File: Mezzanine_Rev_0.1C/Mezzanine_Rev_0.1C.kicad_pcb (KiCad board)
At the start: 2 copper layers, 170 x 85.1 mm, 62 parts, among them J1 QBUS_DWK_64Pin_MBT, J2 DIP20 Header, J3 DIP20 Header, J4 IDC-64M, J5 IDC-16M, J6 IDC-20M, J7 Conn_01x03_Pin, J8 PLD-16R, U1 1533LI1, U10 74LS07, U11 74LS74, U2 1533TM2, U3 1533LA8, U4 CD74HCT4067M, U5 1533LE4, U6 1533AP6, U7 1533AP6, U8 74LS07, U9 74LS07

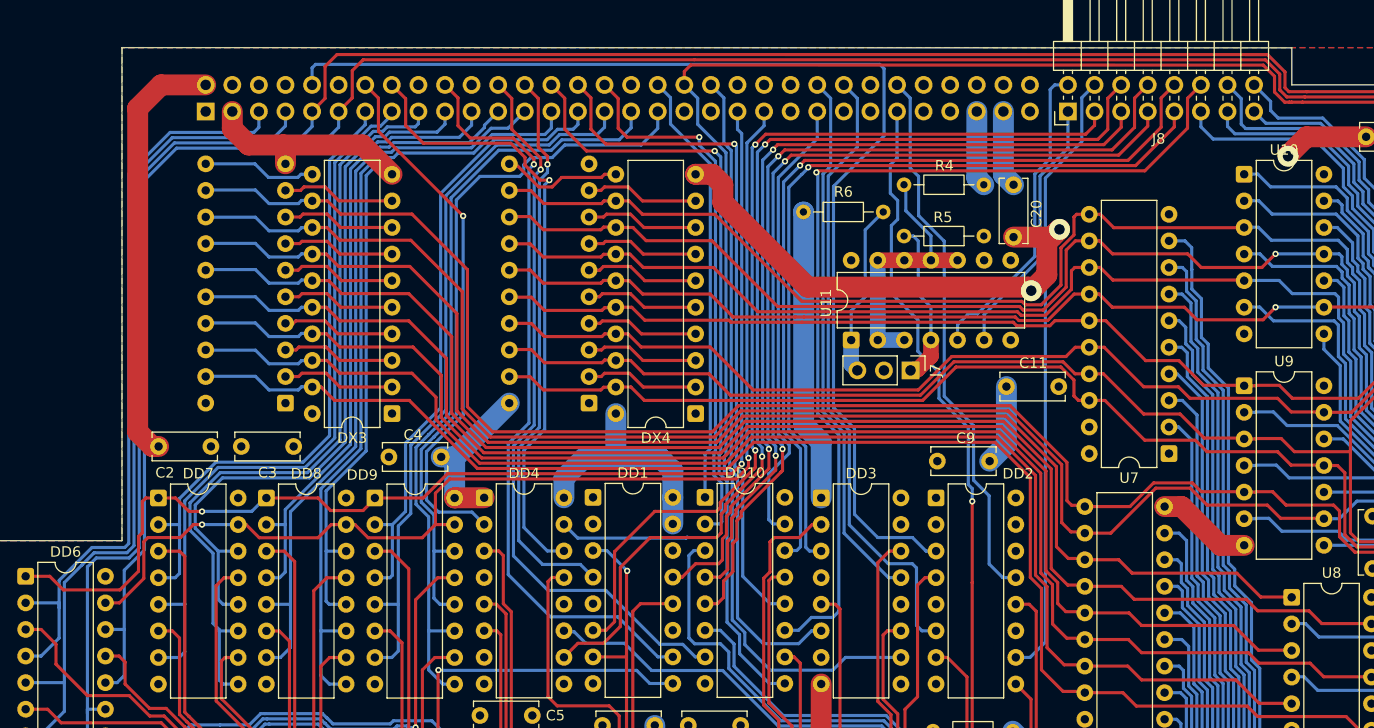
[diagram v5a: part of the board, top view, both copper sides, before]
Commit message: Mezzanine: More layout improvements
Repositioned DX4, allowing for further power tracks connectivity improvements.
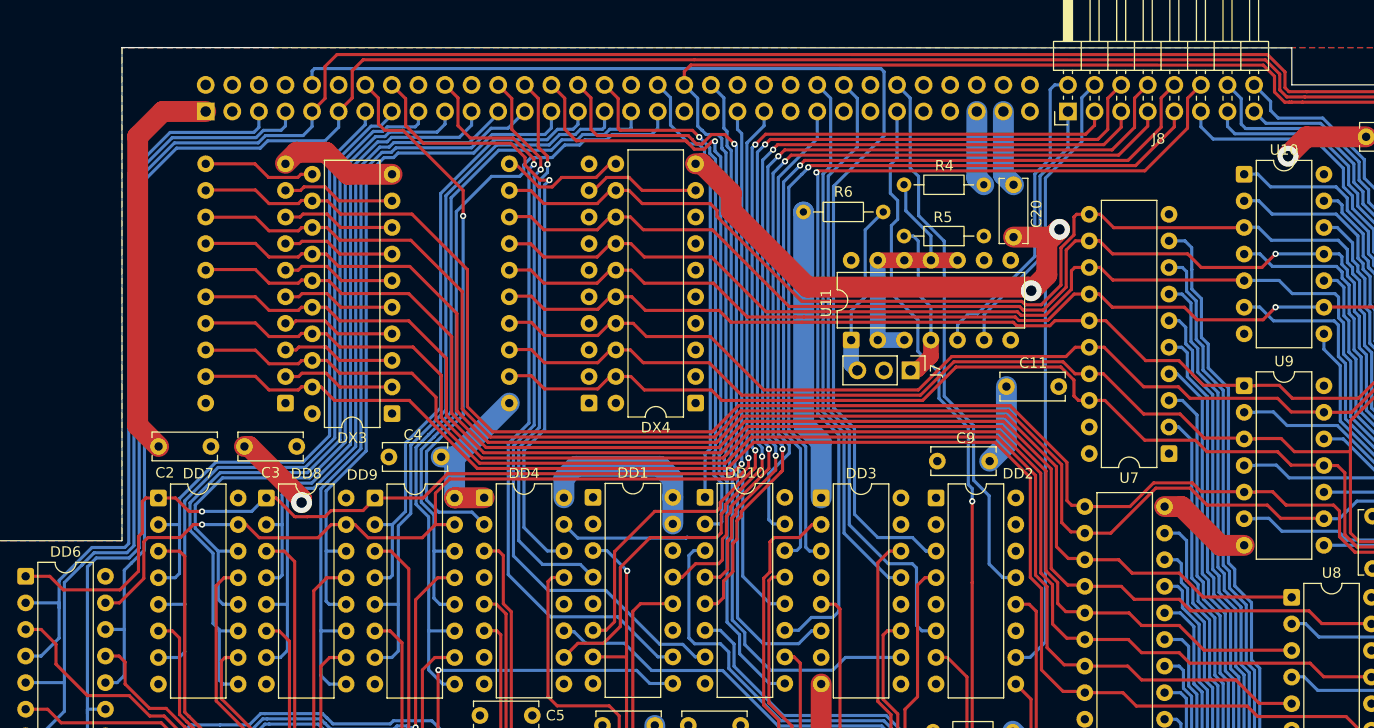
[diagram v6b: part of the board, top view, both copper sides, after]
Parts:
- moved DX4 1.00 mm to (116.2, 78.8)
- moved C3 0.30 mm to (78.1, 82.9)
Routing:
- net Net-(DX4-D4): track 10.9 -> 0.00 mm
- net Net-(DX4-D0): track 10.8 -> 0.00 mm
- net Net-(DX4-D3): track 10.8 -> 0.00 mm
- net Net-(DX4-D1): track 10.8 -> 0.00 mm
- net Net-(DX4-D6): track 10.8 -> 0.00 mm
- net Net-(DX4-D2): track 10.8 -> 0.00 mm
- net Net-(DX4-D5): track 10.8 -> 0.00 mm
- net VCC: track 119.3 -> 109.7 mm
- net GND: track 249.4 -> 245.6 mm, vias 3 -> 4
- net /~{DIN}: track 74.6 -> 75.8 mm
- net /~{A15}: track 154.6 -> 155.8 mm
- net /~{DCLO}: track 51.4 -> 52.5 mm
- net /~{A12}: track 132.0 -> 132.8 mm
- net /~{A9}: track 186.4 -> 187.3 mm
- net /~{A8}: track 136.1 -> 137.0 mm
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
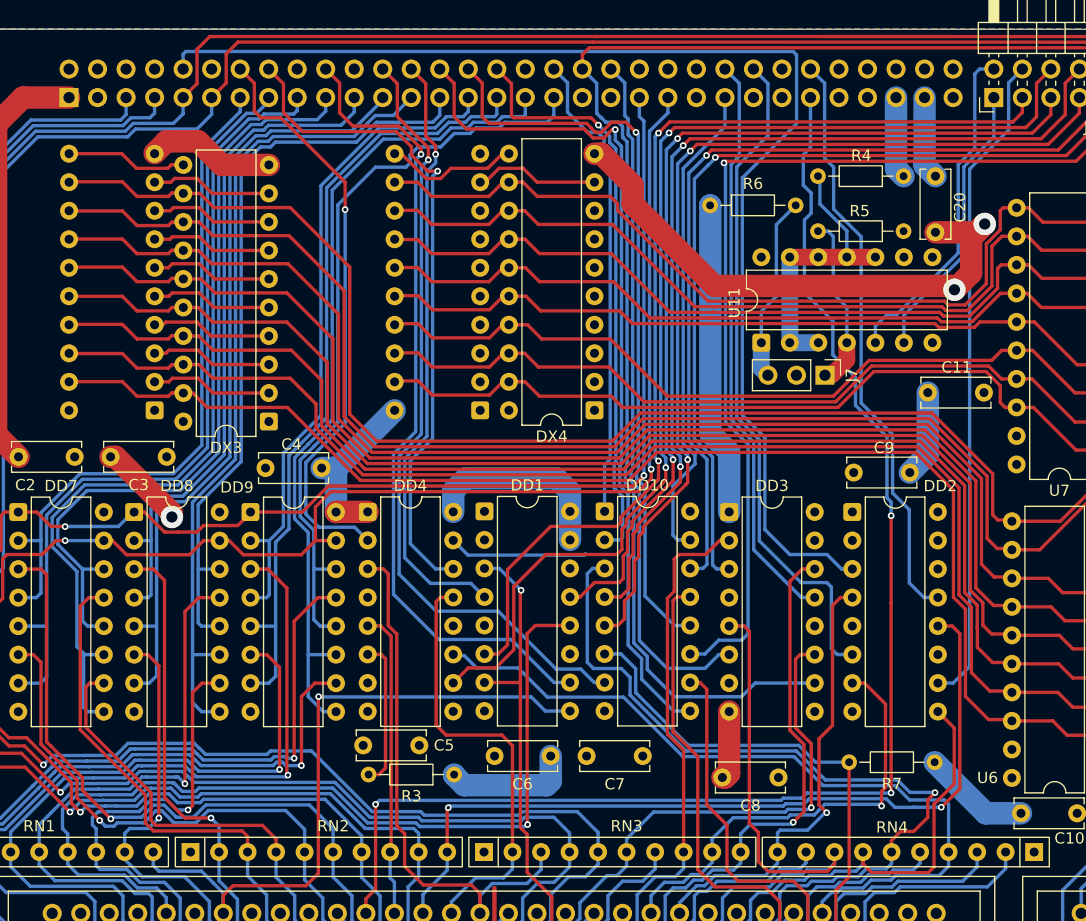
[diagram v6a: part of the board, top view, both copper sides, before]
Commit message: Mezzanine: Adjust J4 position
Better fits the mainboard.
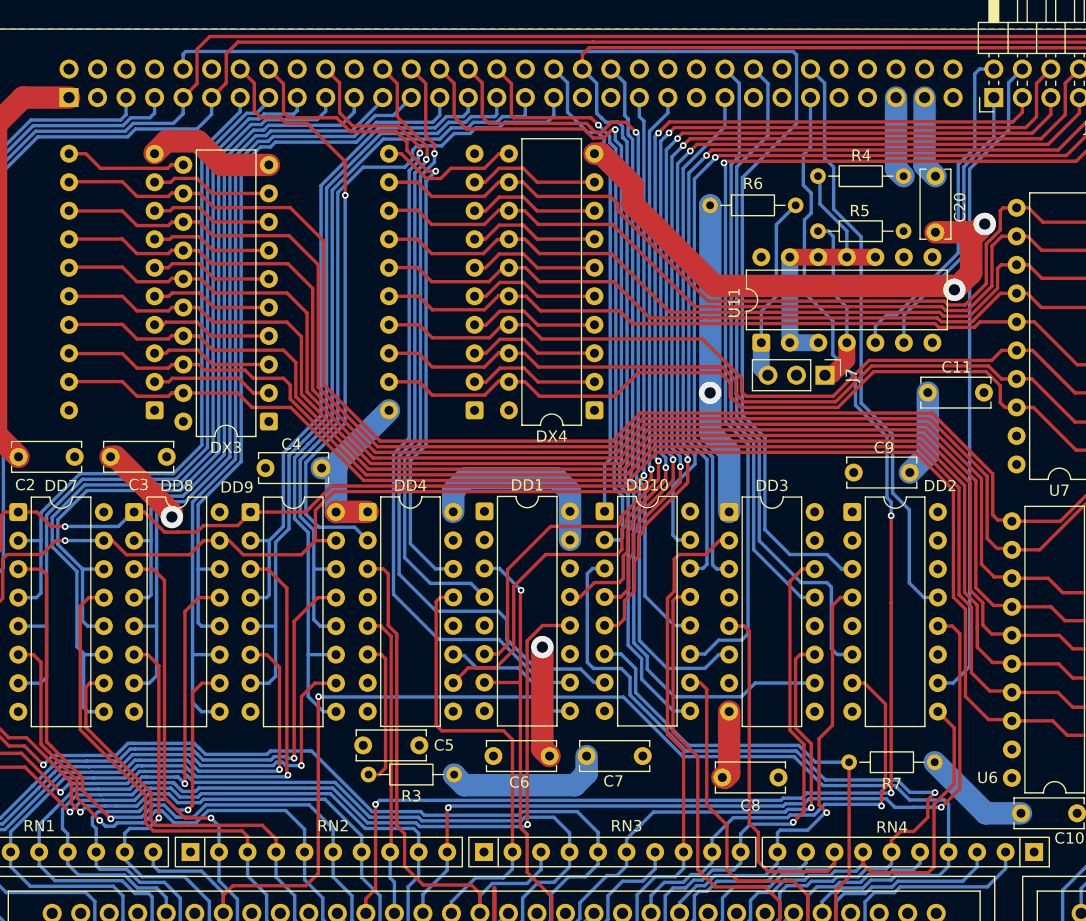
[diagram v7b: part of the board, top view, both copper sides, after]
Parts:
- moved C6 5.10 mm to (107.2, 109.6), turned to 0 degrees
- moved C7 5.00 mm to (115.5, 109.6), turned to 0 degrees
- moved J3 0.50 mm to (105.5, 78.8)
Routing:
- net Net-(DX4-D3): track 0.00 -> 11.7 mm
- net Net-(DX4-D0): track 0.00 -> 11.7 mm
- net Net-(DX4-D6): track 0.00 -> 11.7 mm
- net Net-(DX4-D5): track 0.00 -> 11.7 mm
- net Net-(DX4-D2): track 0.00 -> 11.7 mm
- net Net-(DX4-D1): track 0.00 -> 11.7 mm
- net Net-(DX4-D4): track 0.00 -> 11.7 mm
- net /~{A8}: track 137.0 -> 139.9 mm
- net VCC: track 109.7 -> 112.3 mm, vias 0 -> 1
- net GND: track 245.6 -> 243.2 mm, vias 4 -> 5
- net /~{A9}: track 187.3 -> 188.5 mm
- net Net-(DX4-Cp): track 11.4 -> 12.5 mm
- net /~{DCLO}: track 52.5 -> 53.6 mm
- net /~{DOUT}: track 70.0 -> 71.0 mm
- net /~{AD15}: track 67.6 -> 68.3 mm
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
